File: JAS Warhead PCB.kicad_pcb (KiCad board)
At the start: 2 copper layers, 7 parts, among them J1 Conn_01x15_Socket, J2 Conn_01x15_Socket, J3 Conn_01x02_Socket, J4 Conn_01x02_Socket, J5 Conn_01x02_Socket, J6 Conn_01x02_Socket, J7 Conn_01x02_Socket

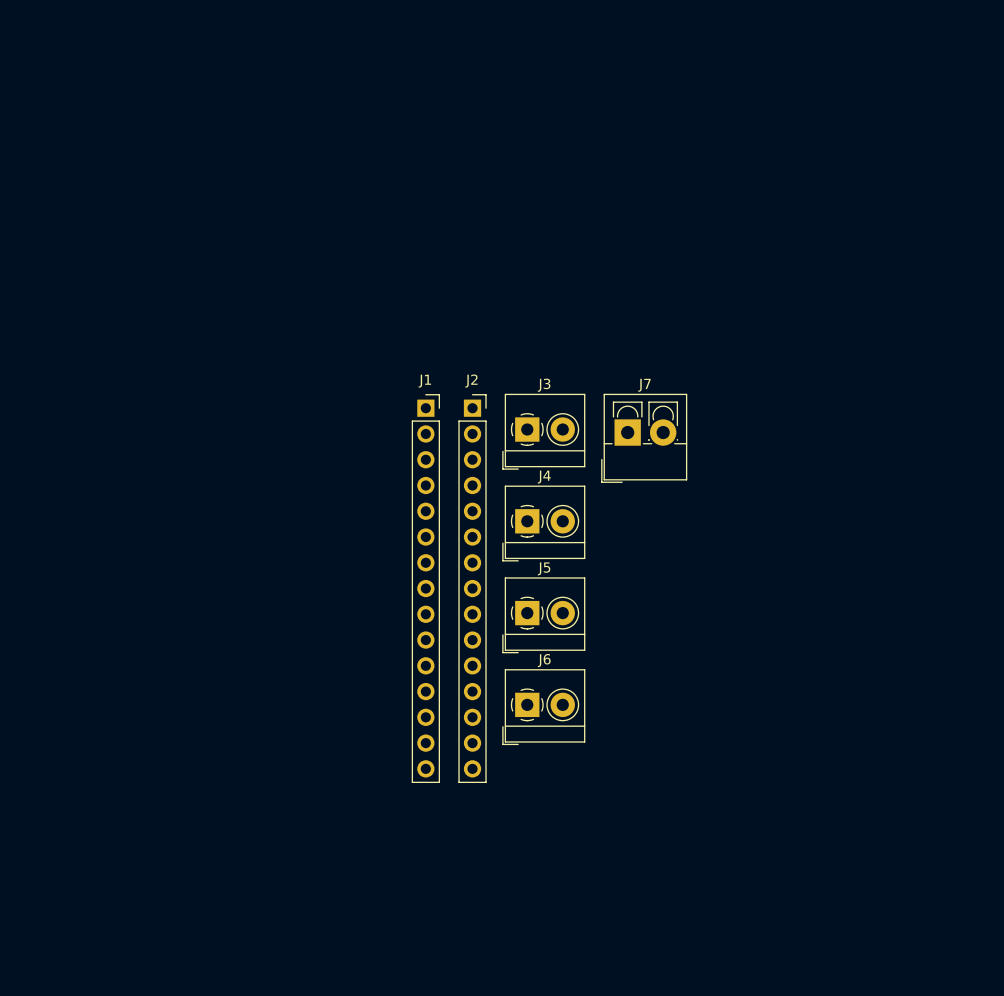
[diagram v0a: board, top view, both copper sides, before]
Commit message: finalizes MAX boards & Begins PCB Design
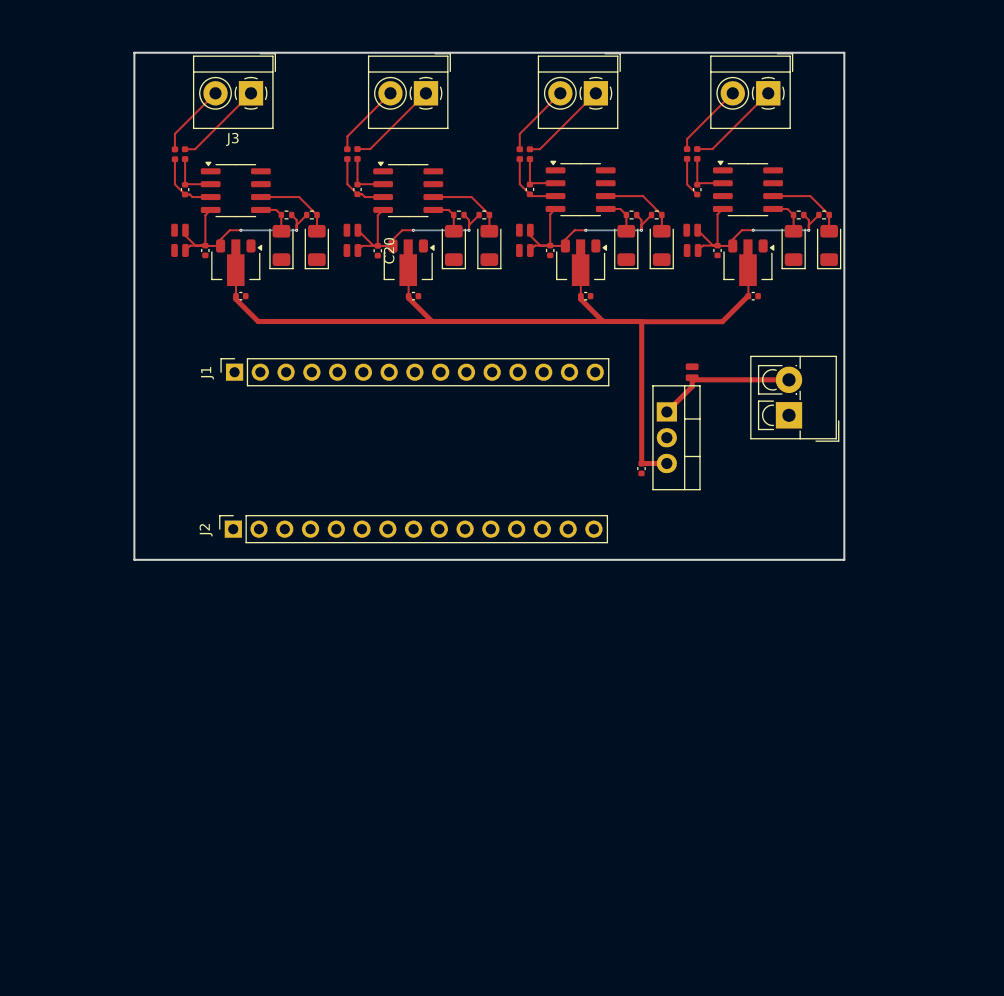
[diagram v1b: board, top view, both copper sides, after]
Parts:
- added C1: 3.3uF, Capacitor_SMD:C_0504_1310Metric, F.Cu at (155.0, 81.5)
- added C10: 1uF, Capacitor_SMD:C_0402_1005Metric, F.Cu at (141.0, 69.5)
- added C11: 10uF, Capacitor_SMD:C_0504_1310Metric, F.Cu at (138.5, 67.5)
- added C12: 10uF, Capacitor_SMD:C_0504_1310Metric, F.Cu at (138.5, 69.5)
- added C13: 1uF, Capacitor_SMD:C_0402_1005Metric, F.Cu at (161.0, 74.0)
- added C14: 0.01uF, Capacitor_SMD:C_0402_1005Metric, F.Cu at (155.5, 63.5)
- added C15: 1uF, Capacitor_SMD:C_0402_1005Metric, F.Cu at (157.5, 69.5)
- added C16: 10uF, Capacitor_SMD:C_0504_1310Metric, F.Cu at (155.0, 69.5)
- added C17: 10uF, Capacitor_SMD:C_0504_1310Metric, F.Cu at (155.0, 67.5)
- added C18: 1uF, Capacitor_SMD:C_0402_1005Metric, F.Cu at (127.5, 74.0)
- added C19: 0.01uF, Capacitor_SMD:C_0402_1005Metric, F.Cu at (122.0, 63.5)
- added C2: 0.2uF, Capacitor_SMD:C_0402_1005Metric, F.Cu at (150.0, 91.0)
- added C20: 1uF, Capacitor_SMD:C_0402_1005Metric, F.Cu at (124.0, 69.5)
- added C21: 10uF, Capacitor_SMD:C_0504_1310Metric, F.Cu at (121.5, 69.5)
- added C22: 10uF, Capacitor_SMD:C_0504_1310Metric, F.Cu at (121.5, 67.5)
- added C23: 0.01uF, Capacitor_SMD:C_0402_1005Metric, F.Cu at (105.0, 63.5)
- added C3: 1uF, Capacitor_SMD:C_0402_1005Metric, F.Cu at (110.5, 74.0)
- added C4: 1uF, Capacitor_SMD:C_0402_1005Metric, F.Cu at (107.0, 69.5)
- added C5: 1uF, Capacitor_SMD:C_0402_1005Metric, F.Cu at (144.5, 74.0)
- added C6: 10uF, Capacitor_SMD:C_0504_1310Metric, F.Cu at (104.5, 69.5)
- added C7: 10uF, Capacitor_SMD:C_0504_1310Metric, F.Cu at (104.5, 67.5)
- added C9: 0.01uF, Capacitor_SMD:C_0402_1005Metric, F.Cu at (139.0, 63.5)
- added D2: 1N4148, Diode_SMD:D_1206_3216Metric, F.Cu at (118.0, 69.0)
- added D3: 1N4148, Diode_SMD:D_1206_3216Metric, F.Cu at (114.5, 69.0)
- added D4: 1N4148, Diode_SMD:D_1206_3216Metric, F.Cu at (152.0, 69.0)
- added D5: 1N4148, Diode_SMD:D_1206_3216Metric, F.Cu at (165.0, 69.0)
- added D6: 1N4148, Diode_SMD:D_1206_3216Metric, F.Cu at (168.5, 69.0)
- added D7: 1N4148, Diode_SMD:D_1206_3216Metric, F.Cu at (131.5, 69.0)
- added D8: 1N4148, Diode_SMD:D_1206_3216Metric, F.Cu at (135.0, 69.0)
- added D9: 1N4148, Diode_SMD:D_1206_3216Metric, F.Cu at (148.5, 69.0)
- added FB1: FerriteBead, Inductor_SMD:L_0402_1005Metric, F.Cu at (104.0, 60.0)
- added FB2: FerriteBead, Inductor_SMD:L_0402_1005Metric, F.Cu at (139.0, 60.0)
- added FB4: FerriteBead, Inductor_SMD:L_0402_1005Metric, F.Cu at (105.0, 60.0)
- added FB5: FerriteBead, Inductor_SMD:L_0402_1005Metric, F.Cu at (154.5, 60.0)
- added FB6: FerriteBead, Inductor_SMD:L_0402_1005Metric, F.Cu at (155.5, 60.0)
- added FB7: FerriteBead, Inductor_SMD:L_0402_1005Metric, F.Cu at (121.0, 60.0)
- added FB8: FerriteBead, Inductor_SMD:L_0402_1005Metric, F.Cu at (122.0, 60.0)
- added FB9: FerriteBead, Inductor_SMD:L_0402_1005Metric, F.Cu at (138.0, 60.0)
- added R2: 10K, Resistor_SMD:R_0402_1005Metric, F.Cu at (117.5, 66.0)
- added R3: 10K, Resistor_SMD:R_0402_1005Metric, F.Cu at (115.0, 66.0)
- added R4: 10K, Resistor_SMD:R_0402_1005Metric, F.Cu at (151.5, 66.0)
- added R5: 10K, Resistor_SMD:R_0402_1005Metric, F.Cu at (165.5, 66.0)
- added R6: 10K, Resistor_SMD:R_0402_1005Metric, F.Cu at (168.0, 66.0)
- added R7: 10K, Resistor_SMD:R_0402_1005Metric, F.Cu at (132.0, 66.0)
- added R8: 10K, Resistor_SMD:R_0402_1005Metric, F.Cu at (134.5, 66.0)
- added R9: 10K, Resistor_SMD:R_0402_1005Metric, F.Cu at (149.0, 66.0)
- added U1: LM7805_TO220, Package_TO_SOT_THT:TO-220-3_Vertical, F.Cu at (152.5, 85.4)
- added U10: AP2127R-3.3, Package_TO_SOT_SMD:SOT-89-3, F.Cu at (160.5, 71.0)
- added U2: AP2127R-3.3, Package_TO_SOT_SMD:SOT-89-3, F.Cu at (144.0, 71.0)
- added U3: AP2127R-3.3, Package_TO_SOT_SMD:SOT-89-3, F.Cu at (110.0, 71.0)
- added U5: MAX31855KASA, Package_SO:SOIC-8_3.9x4.9mm_P1.27mm, F.Cu at (110.0, 63.6)
- added U6: MAX31855KASA, Package_SO:SOIC-8_3.9x4.9mm_P1.27mm, F.Cu at (144.0, 63.5)
- added U7: MAX31855KASA, Package_SO:SOIC-8_3.9x4.9mm_P1.27mm, F.Cu at (160.5, 63.5)
- added U8: AP2127R-3.3, Package_TO_SOT_SMD:SOT-89-3, F.Cu at (127.0, 71.0)
- added U9: MAX31855KASA, Package_SO:SOIC-8_3.9x4.9mm_P1.27mm, F.Cu at (127.0, 63.6)
- moved J6 61.1 mm to (128.8, 54.0), turned to 180 degrees
- moved J5 56.5 mm to (162.5, 54.0), turned to 180 degrees
- moved J3 42.9 mm to (111.5, 54.0), turned to 180 degrees
- moved J4 42.7 mm to (145.5, 54.0), turned to 180 degrees
- moved J2 26.4 mm to (109.8, 97.0), turned to 90 degrees
- moved J1 19.2 mm to (109.9, 81.5), turned to 90 degrees
- moved J7 16.0 mm to (164.5, 85.8), turned to 90 degrees
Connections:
- J3 pad 1: unconnected-(J3-Pin_1-Pad1) -> Net-(J3-Pin_1)
- J3 pad 2: unconnected-(J3-Pin_2-Pad2) -> Net-(J3-Pin_2)
- J4 pad 1: unconnected-(J4-Pin_1-Pad1) -> Net-(J4-Pin_1)
- J4 pad 2: unconnected-(J4-Pin_2-Pad2) -> Net-(J4-Pin_2)
- J5 pad 1: unconnected-(J5-Pin_1-Pad1) -> Net-(J5-Pin_1)
- J5 pad 2: unconnected-(J5-Pin_2-Pad2) -> Net-(J5-Pin_2)
- J6 pad 1: unconnected-(J6-Pin_1-Pad1) -> Net-(J6-Pin_1)
- J6 pad 2: unconnected-(J6-Pin_2-Pad2) -> Net-(J6-Pin_2)
- J7 pad 1: unconnected-(J7-Pin_1-Pad1) -> GND
- J7 pad 2: unconnected-(J7-Pin_2-Pad2) -> +12V
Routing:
- net +5V: track 0.00 -> 95.6 mm
- net +3V3: track 0.00 -> 91.0 mm, vias 0 -> 8
- net +12V: track 0.00 -> 14.0 mm
- net Net-(J5-Pin_1): track 0.00 -> 9.28 mm
- net Net-(J6-Pin_1): track 0.00 -> 9.03 mm
- net Net-(J4-Pin_1): track 0.00 -> 8.78 mm
- net Net-(J3-Pin_1): track 0.00 -> 8.78 mm
- net Net-(D4-A): track 0.00 -> 7.91 mm
- net Net-(D6-A): track 0.00 -> 7.91 mm
- net Net-(D2-A): track 0.00 -> 7.88 mm
- net Net-(D8-A): track 0.00 -> 7.87 mm
- net Net-(J5-Pin_2): track 0.00 -> 7.36 mm
- net Net-(J6-Pin_2): track 0.00 -> 7.28 mm
- net Net-(J3-Pin_2): track 0.00 -> 7.19 mm
- net Net-(J4-Pin_2): track 0.00 -> 7.17 mm
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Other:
- board outline added: 70 x 50 mm

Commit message: merge labels
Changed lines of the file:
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@@
 		(tags "Through hole socket strip THT 1x15 2.54mm single row")
 		(property "Reference" "J2"
-			(at 0 -2.77 270)
+			(at 0 -2.77 -90)
 			(layer "F.SilkS")
 			(effects
@@
 		)
 		(property "Value" "Conn_01x15_Socket"
-			(at 0 38.33 270)
+			(at 0 38.33 -90)
 			(layer "F.Fab")
 			(hide yes)
@@
 		)
 		(fp_text user "${REFERENCE}"
-			(at 0 17.78 360)
+			(at 0 17.78 0)
 			(layer "F.Fab")
 			(effects
@@
 		(tags "diode")
 		(property "Reference" "D2"
-			(at 0 -1.82 270)
+			(at 0 -1.82 -90)
 			(layer "F.SilkS")
 			(hide yes)
@@
 		)
 		(property "Value" "1N4148"
-			(at 0 1.82 270)
+			(at 0 1.82 -90)
 			(layer "F.Fab")
 			(hide yes)
@@
 		)
 		(fp_text user "${REFERENCE}"
-			(at 0 0 270)
+			(at 0 0 -90)
 			(layer "F.Fab")
 			(effects
@@
 		(tags "diode")
 		(property "Reference" "D3"
-			(at 0 -1.82 270)
+			(at 0 -1.82 -90)
 			(layer "F.SilkS")
 			(hide yes)
@@
 		)
 		(property "Value" "1N4148"
-			(at 0 1.82 270)
+			(at 0 1.82 -90)
 			(layer "F.Fab")
 			(hide yes)
@@
 		)
 		(fp_text user "${REFERENCE}"
-			(at 0 0 270)
+			(at 0 0 -90)
 			(layer "F.Fab")
 			(effects
@@
 		(tags "capacitor")
 		(property "Reference" "C1"
-			(at 0 -1.49 270)
+			(at 0 -1.49 -90)
 			(layer "F.SilkS")
 			(hide yes)
@@
 		)
 		(property "Value" "3.3uF"
-			(at 0 1.49 270)
+			(at 0 1.49 -90)
 			(layer "F.Fab")
 			(hide yes)
@@
 		)
 		(fp_text user "${REFERENCE}"
-			(at 0 0 270)
+			(at 0 0 -90)
 			(layer "F.Fab")
 			(effects
@@
 		(tags "diode")
 		(property "Reference" "D7"
-			(at 0 -1.82 270)
+			(at 0 -1.82 -90)
 			(layer "F.SilkS")
 			(hide yes)
@@
 		)
 		(property "Value" "1N4148"
-			(at 0 1.82 270)
+			(at 0 1.82 -90)
 			(layer "F.Fab")
 			(hide yes)
@@
 		)
 		(fp_text user "${REFERENCE}"
-			(at 0 0 270)
+			(at 0 0 -90)
 			(layer "F.Fab")
 			(effects
@@
 		(tags "THT Terminal Block 4Ucon ItemNo. 10693 vertical pitch 3.5mm size 8x8.3mm^2 drill 1.3mm pad 2.6mm")
 		(property "Reference" "J7"
-			(at 1.75 -4.76 270)
+			(at 1.75 -4.76 -90)
 			(layer "F.SilkS")
 			(hide yes)
@@
 		)
 		(property "Value" "Conn_01x02_Socket"
-			(at 1.75 5.66 270)
+			(at 1.75 5.66 -90)
 			(layer "F.Fab")
 			(hide yes)
@@
 		)
 		(fp_text user "${REFERENCE}"
-			(at 1.75 3.45 270)
+			(at 1.75 3.45 -90)
 			(layer "F.Fab")
 			(effects
@@
 		(tags "capacitor")
 		(property "Reference" "C9"
-			(at 0 -1.16 270)
+			(at 0 -1.16 -90)
 			(layer "F.SilkS")
 			(hide yes)
@@
 		)
 		(property "Value" "0.01uF"
-			(at 0 1.16 270)
+			(at 0 1.16 -90)
 			(layer "F.Fab")
 			(hide yes)
@@
 		)
 		(fp_text user "${REFERENCE}"
-			(at 0 0 270)
+			(at 0 0 -90)
 			(layer "F.Fab")
 			(effects
@@
 		(tags "diode")
 		(property "Reference" "D9"
-			(at 0 -1.82 270)
+			(at 0 -1.82 -90)
 			(layer "F.SilkS")
 			(hide yes)
@@
 		)
 		(property "Value" "1N4148"
-			(at 0 1.82 270)
+			(at 0 1.82 -90)
 			(layer "F.Fab")
 			(hide yes)
@@
 		)
 		(fp_text user "${REFERENCE}"
-			(at 0 0 270)
+			(at 0 0 -90)
 			(layer "F.Fab")
 			(effects
@@
 		(tags "diode")
 		(property "Reference" "D8"
-			(at 0 -1.82 270)
+			(at 0 -1.82 -90)
 			(layer "F.SilkS")
 			(hide yes)
@@
 		)
 		(property "Value" "1N4148"
-			(at 0 1.82 270)
+			(at 0 1.82 -90)
 			(layer "F.Fab")
 			(hide yes)
@@
 		)
 		(fp_text user "${REFERENCE}"
-			(at 0 0 270)
+			(at 0 0 -90)
 			(layer "F.Fab")
 			(effects
@@
 		(tags "capacitor")
 		(property "Reference" "C23"
-			(at 0 -1.16 270)
+			(at 0 -1.16 -90)
 			(layer "F.SilkS")
 			(hide yes)
@@
 		)
 		(property "Value" "0.01uF"
-			(at 0 1.16 270)
+			(at 0 1.16 -90)
 			(layer "F.Fab")
 			(hide yes)
@@
 		)
 		(fp_text user "${REFERENCE}"
-			(at 0 0 270)
+			(at 0 0 -90)
 			(layer "F.Fab")
 			(effects
@@
 		(tags "capacitor")
 		(property "Reference" "C19"
-			(at 0 -1.16 270)
+			(at 0 -1.16 -90)
 			(layer "F.SilkS")
 			(hide yes)
@@
 		)
 		(property "Value" "0.01uF"
-			(at 0 1.16 270)
+			(at 0 1.16 -90)
 			(layer "F.Fab")
 			(hide yes)
@@
 		)
 		(fp_text user "${REFERENCE}"
-			(at 0 0 270)
+			(at 0 0 -90)
 			(layer "F.Fab")
 			(effects
@@
 		(tags "diode")
 		(property "Reference" "D6"
-			(at 0 -1.82 270)
+			(at 0 -1.82 -90)
 			(layer "F.SilkS")
 			(hide yes)
@@
 		)
 		(property "Value" "1N4148"
-			(at 0 1.82 270)
+			(at 0 1.82 -90)
 			(layer "F.Fab")
 			(hide yes)
@@
 		)
 		(fp_text user "${REFERENCE}"
-			(at 0 0 270)
+			(at 0 0 -90)
 			(layer "F.Fab")
 			(effects
@@
 		(tags "diode")
 		(property "Reference" "D5"
-			(at 0 -1.82 270)
+			(at 0 -1.82 -90)
 			(layer "F.SilkS")
 			(hide yes)
@@
 		)
 		(property "Value" "1N4148"
-			(at 0 1.82 270)
+			(at 0 1.82 -90)
 			(layer "F.Fab")
 			(hide yes)
@@
 		)
 		(fp_text user "${REFERENCE}"
-			(at 0 0 270)
+			(at 0 0 -90)
 			(layer "F.Fab")
 			(effects
@@
 		(tags "Through hole socket strip THT 1x15 2.54mm single row")
 		(property "Reference" "J1"
-			(at 0 -2.77 270)
+			(at 0 -2.77 -90)
 			(layer "F.SilkS")
 			(effects
@@
 		)
 		(property "Value" "Conn_01x15_Socket"
-			(at 0 38.33 270)
+			(at 0 38.33 -90)
 			(layer "F.Fab")
 			(hide yes)
@@
 		)
 		(fp_text user "${REFERENCE}"
-			(at 0 17.78 360)
+			(at 0 17.78 0)
 			(layer "F.Fab")
 			(effects
@@
 		(tags "capacitor")
 		(property "Reference" "C14"
-			(at 0 -1.16 270)
+			(at 0 -1.16 -90)
 			(layer "F.SilkS")
 			(hide yes)
@@
 		)
 		(property "Value" "0.01uF"
-			(at 0 1.16 270)
+			(at 0 1.16 -90)
 			(layer "F.Fab")
 			(hide yes)
@@
 		)
 		(fp_text user "${REFERENCE}"
-			(at 0 0 270)
+			(at 0 0 -90)
 			(layer "F.Fab")
 			(effects
@@
 			(at 0 -1.16 90)
 			(layer "F.SilkS")
+			(hide yes)
 			(effects
 				(font
@@
 		(tags "diode")
 		(property "Reference" "D4"
-			(at 0 -1.82 270)
+			(at 0 -1.82 -90)
 			(layer "F.SilkS")
 			(hide yes)
@@
 		)
 		(property "Value" "1N4148"
-			(at 0 1.82 270)
+			(at 0 1.82 -90)
 			(layer "F.Fab")
 			(hide yes)
@@
 		)
 		(fp_text user "${REFERENCE}"
-			(at 0 0 270)
+			(at 0 0 -90)
 			(layer "F.Fab")
 			(effects

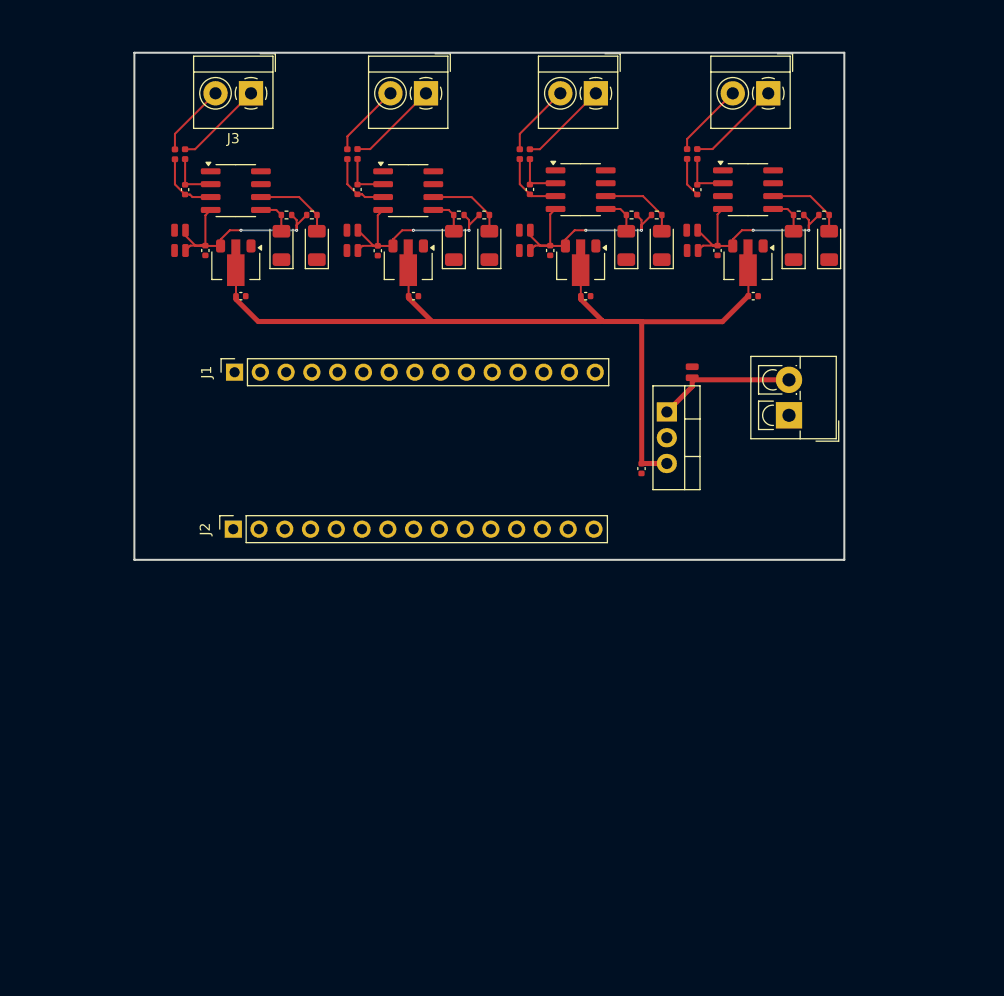
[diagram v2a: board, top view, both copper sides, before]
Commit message: PCB Wiring to ESP32
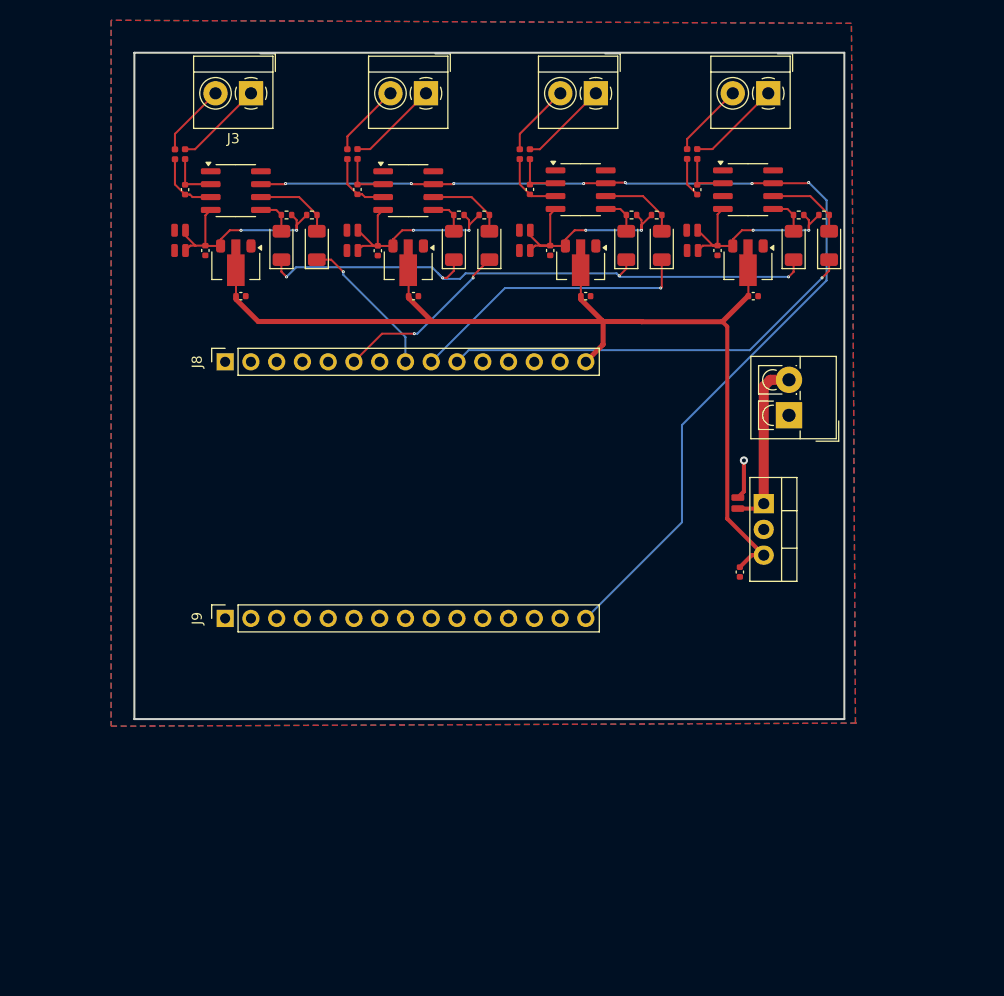
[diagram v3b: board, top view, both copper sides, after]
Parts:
- removed J1, J2: Conn_01x15_Socket, Connector_PinSocket_2.54mm:PinSocket_1x15_P2.54mm_Vertical
- added J8: Conn_01x15_Socket, Connector_PinSocket_2.54mm:PinSocket_1x15_P2.54mm_Vertical, F.Cu at (109.0, 80.5)
- added J9: Conn_01x15_Socket, Connector_PinSocket_2.54mm:PinSocket_1x15_P2.54mm_Vertical, F.Cu at (109.0, 105.8)
- moved C2 14.1 mm to (159.7, 101.2)
- moved C1 13.7 mm to (159.5, 94.4)
- moved U1 13.2 mm to (162.1, 94.5)
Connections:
- D2 pad 1: /MAX6675 K-Type Thermocouple Amp 1/CS -> /CS1
- D3 pad 1: /MAX6675 K-Type Thermocouple Amp 1/SCK -> /SPI CLK
- D4 pad 1: /MAX6675 K-Type Thermocouple Amp 2/CS -> /CS2
- D5 pad 1: /MAX6675 K-Type Thermocouple Amp 3/SCK -> /SPI CLK
- D6 pad 1: /MAX6675 K-Type Thermocouple Amp 3/CS -> /CS3
- D7 pad 1: /MAX6675 K-Type Thermocouple Amp 4/SCK -> /SPI CLK
- D8 pad 1: /MAX6675 K-Type Thermocouple Amp 4/CS -> /CS4
- D9 pad 1: /MAX6675 K-Type Thermocouple Amp 2/SCK -> /SPI CLK
- U5 pad 7: /MAX6675 K-Type Thermocouple Amp 1/DO -> /SPI Data_In
- U6 pad 7: /MAX6675 K-Type Thermocouple Amp 2/DO -> /SPI Data_In
- U7 pad 7: /MAX6675 K-Type Thermocouple Amp 3/DO -> /SPI Data_In
- U9 pad 7: /MAX6675 K-Type Thermocouple Amp 4/DO -> /SPI Data_In
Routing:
- net /SPI Data_In: track 0.00 -> 107.9 mm, vias 0 -> 7
- net /SPI CLK: track 0.00 -> 59.6 mm, vias 0 -> 4
- net /CS3: track 0.00 -> 41.5 mm, vias 0 -> 1
- net /CS2: track 0.00 -> 28.5 mm, vias 0 -> 1
- net /CS4: track 0.00 -> 17.6 mm, vias 0 -> 2
- net +5V: track 95.6 -> 111.3 mm
- net /CS1: track 0.00 -> 14.5 mm, vias 0 -> 1
- net GND: track 0.00 -> 3.91 mm, vias 0 -> 1
- net +12V: track 14.0 -> 17.1 mm
- net +3V3: track 91.0 -> 89.6 mm
- added copper zone on B.Cu, net GND
- added copper zone on F.Cu, net GND
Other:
- board size 70 x 50 mm -> 70 x 65.7 mm
